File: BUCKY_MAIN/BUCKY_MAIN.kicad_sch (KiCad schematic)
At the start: 23 parts

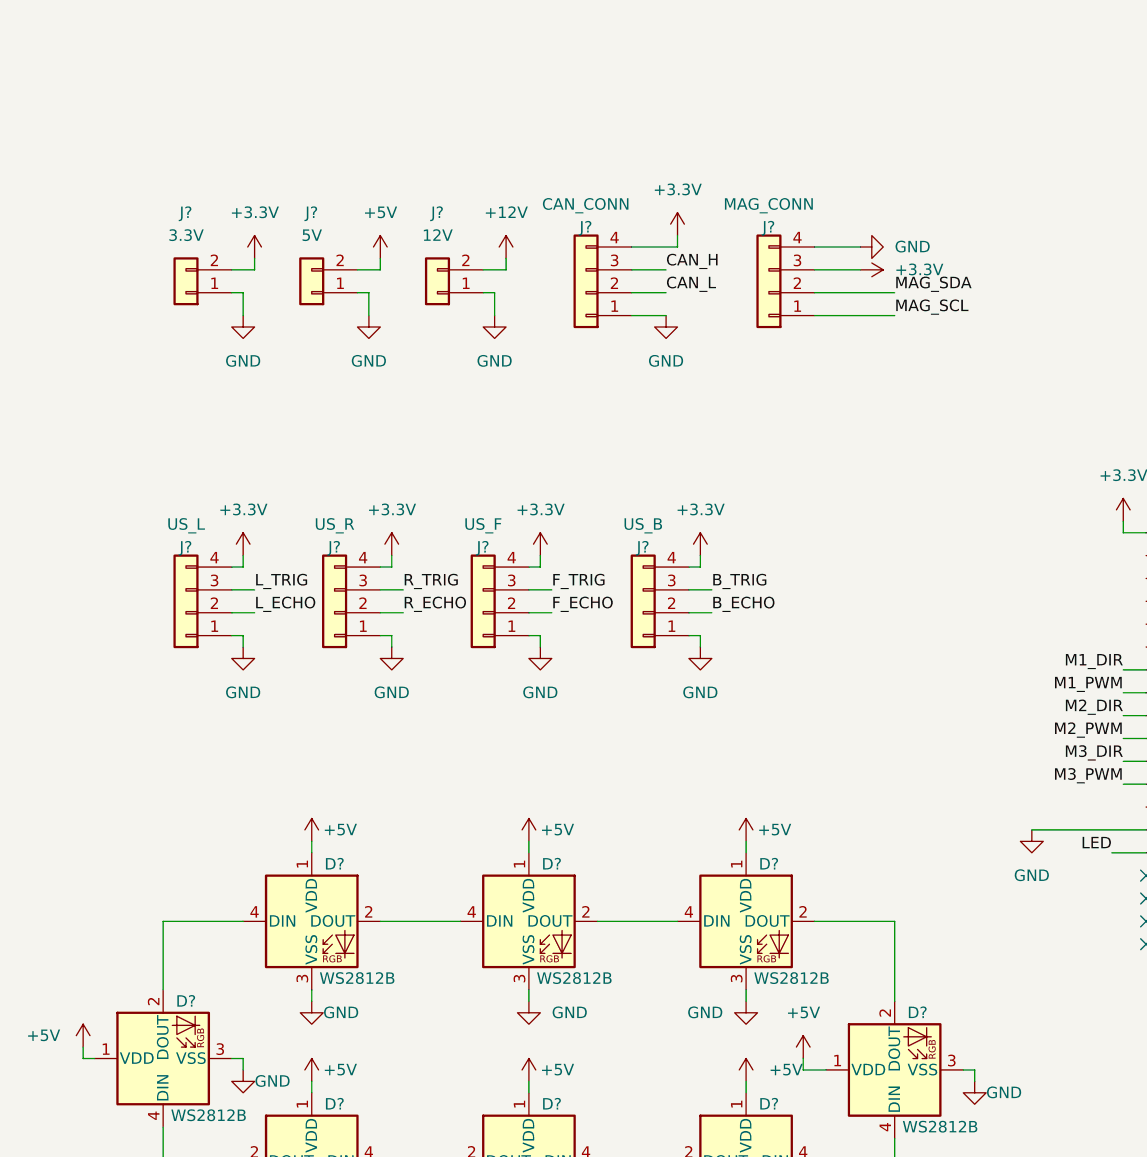
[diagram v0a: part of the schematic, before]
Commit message: Finished Motor Driver Brd
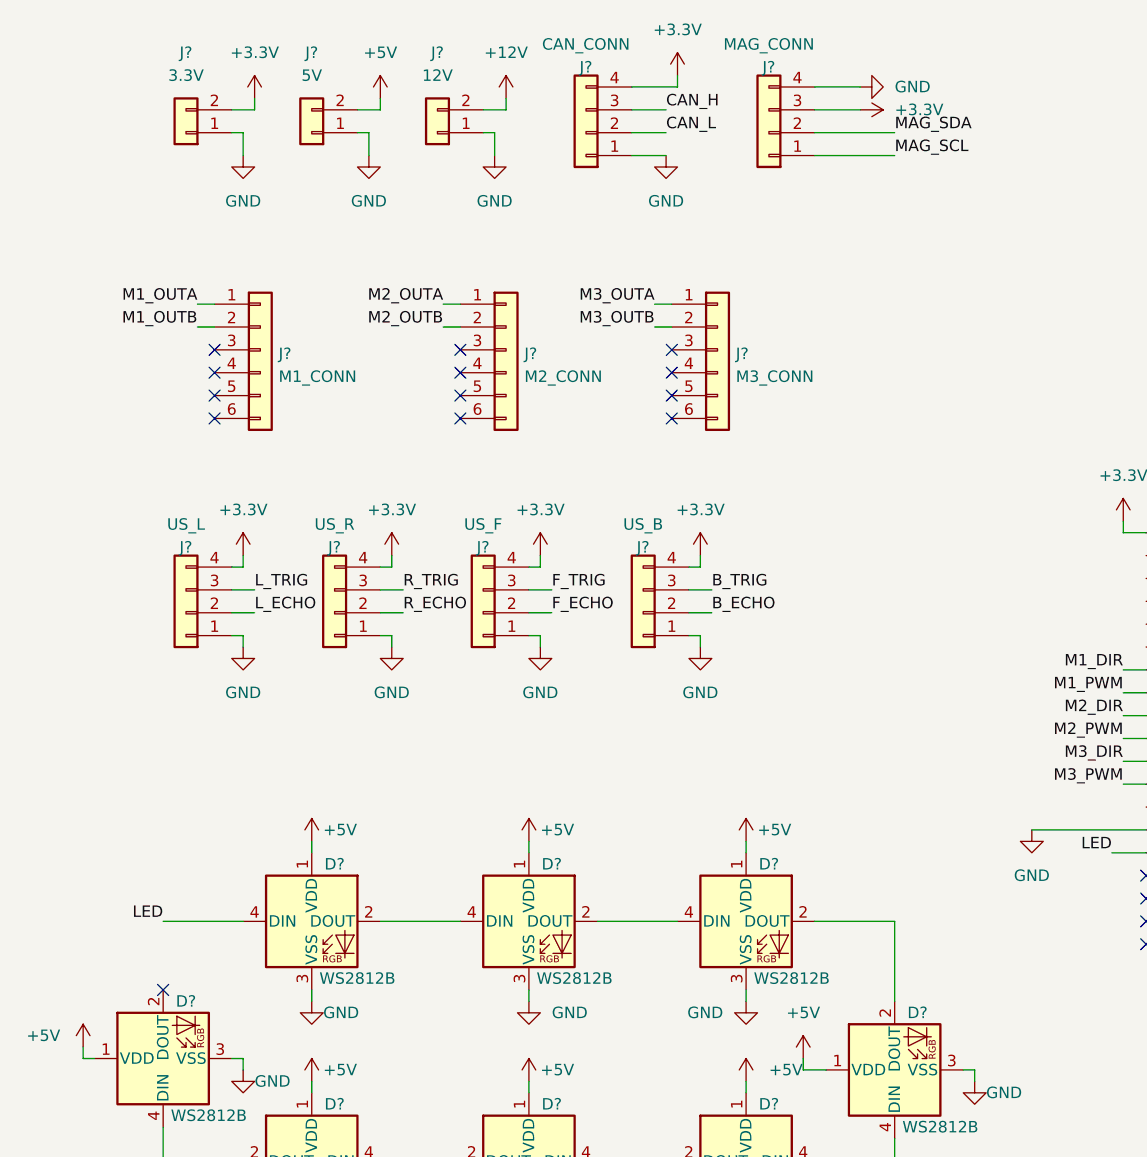
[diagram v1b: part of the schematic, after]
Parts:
- added J?: M3_CONN, symbol Connector_Generic:Conn_01x06
- added J?: M2_CONN, symbol Connector_Generic:Conn_01x06
- added J?: M1_CONN, symbol Connector_Generic:Conn_01x06
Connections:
- net LED: now also D?.4 (DIN)
- net M1_OUTA: now also J?.1 (Pin_1)
- net M1_OUTB: now also J?.2 (Pin_2)
- net M2_OUTA: now also J?.1 (Pin_1)
- net M2_OUTB: now also J?.2 (Pin_2)
- net M3_OUTA: now also J?.1 (Pin_1)
- net M3_OUTB: now also J?.2 (Pin_2)
- net at D?.2 (DOUT): no longer D?.4 (DIN)
- no-connect marks 22 -> 35
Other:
- moved on the sheet: J?

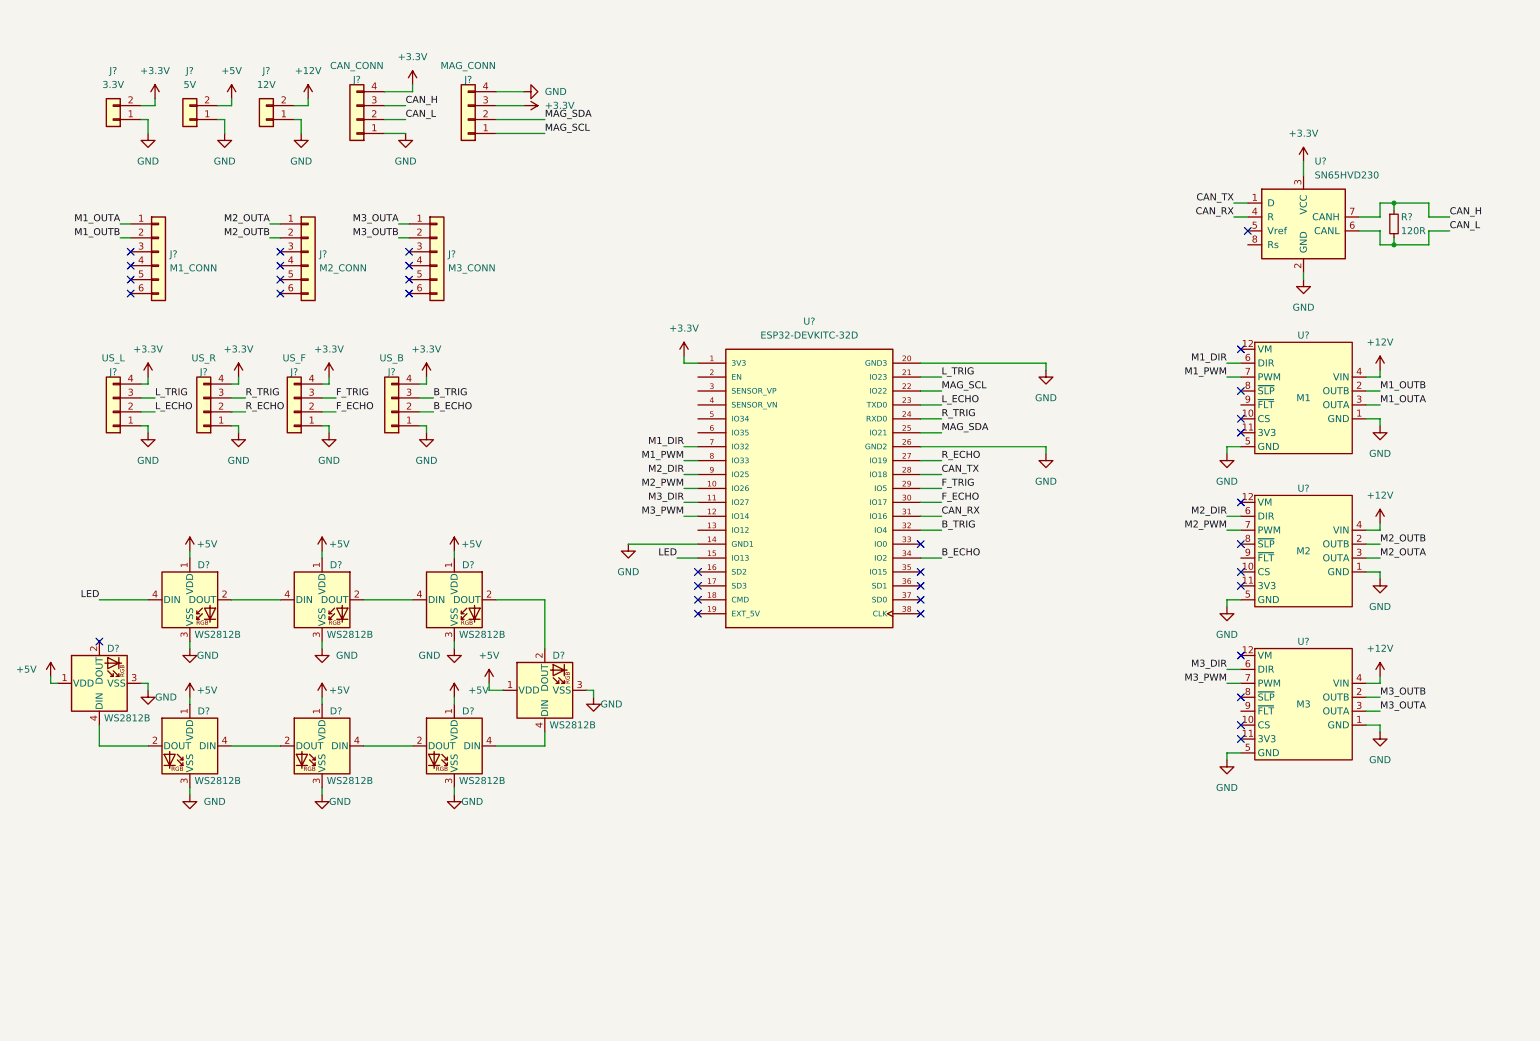
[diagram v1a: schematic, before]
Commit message: Finished up IR sch, Main, Started Power
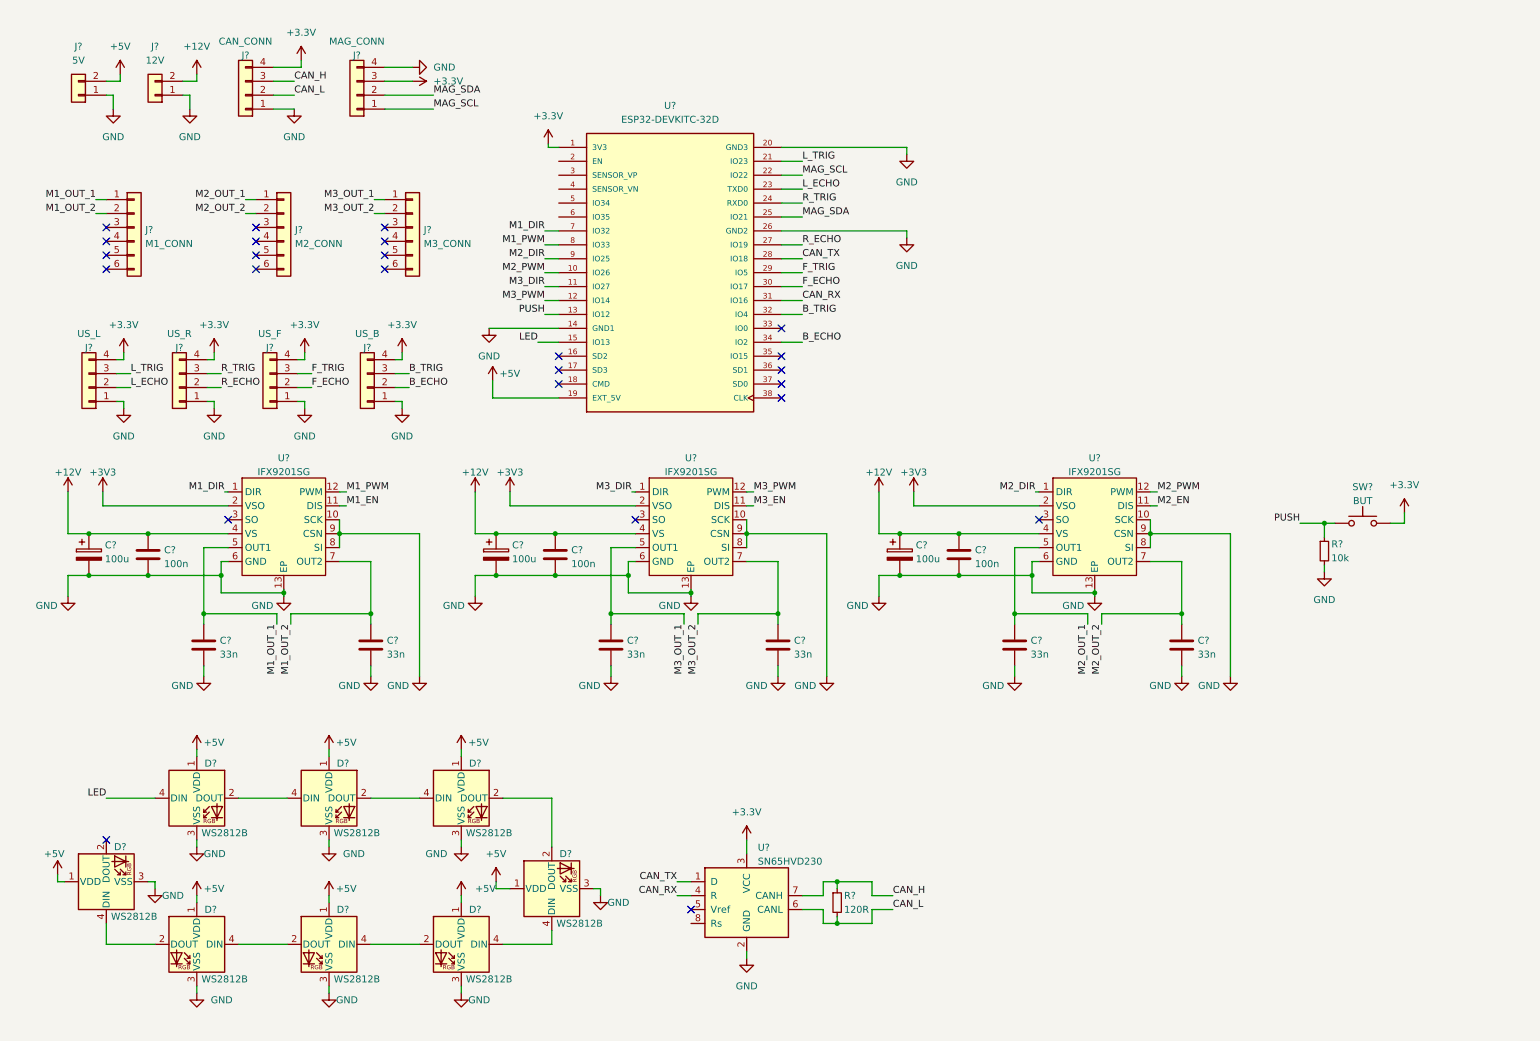
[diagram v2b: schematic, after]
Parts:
- removed J?: 3.3V, symbol Connector_Generic:Conn_01x02
- removed U?: M2, symbol BUCKY_MAIN:G2-24v13
- removed U?: M1, symbol BUCKY_MAIN:G2-24v13
- removed U?: M3, symbol BUCKY_MAIN:G2-24v13
- added C? (x6): 33n, Capacitor_SMD:C_0603_1608Metric_Pad1.08x0.95mm_HandSolder, symbol Device:C
- added C? (x3): 100u, Capacitor_SMD:CP_Elec_6.3x7.7, symbol Device:C_Polarized
- added C? (x3): 100n, Capacitor_SMD:C_0805_2012Metric_Pad1.18x1.45mm_HandSolder, symbol Device:C
- added R?: 10k, symbol Device:R_Small
- added SW?: BUT, symbol Switch:SW_Push
- added U? (x3): IFX9201SG, Package_SO:Infineon_PG-DSO-12-11_ThermalVias, symbol BUCKY_MOTOR_DRIVER:IFX9201SG
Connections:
- net +12V: now also C?.1, C?.1, C?.1, C?.1, C?.1, C?.1, U?.4 (VS), U?.4 (VS), U?.4 (VS)
- net +3.3V: now also SW?.2
- net +5V: now also U?.19 (EXT_5V)
- net GND: now also C?.2, C?.2, C?.2, C?.2, C?.2, C?.2, C?.2, C?.2, C?.2, C?.2, C?.2, C?.2, R?.2, U?.10 (SCK), U?.10 (SCK), U?.10 (SCK), U?.13 (EP), U?.13 (EP), U?.13 (EP), U?.6 (GND), U?.6 (GND), U?.6 (GND), U?.8 (SI), U?.8 (SI), U?.8 (SI), U?.9 (CSN), U?.9 (CSN), U?.9 (CSN)
- net M1_DIR: now also U?.1 (DIR)
- net M1_PWM: now also U?.12 (PWM)
- net M2_DIR: now also U?.1 (DIR)
- net M2_PWM: now also U?.12 (PWM)
- net M3_DIR: now also U?.1 (DIR)
- net M3_PWM: now also U?.12 (PWM)
- net PUSH: now reaches U?.13 (IO12)
- net PUSH: now also R?.1, SW?.1
- net M1_OUTA renamed M1_OUT_1
- net M1_OUT_1: now also C?.1, U?.5 (OUT1)
- net M1_OUTB renamed M1_OUT_2
- net M1_OUT_2: now also C?.1, U?.7 (OUT2)
- net M2_OUTA renamed M2_OUT_1
- net M2_OUT_1: now also C?.1, U?.5 (OUT1)
- net M2_OUTB renamed M2_OUT_2
- net M2_OUT_2: now also C?.1, U?.7 (OUT2)
- net M3_OUTA renamed M3_OUT_1
- net M3_OUT_1: now also C?.1, U?.5 (OUT1)
- net M3_OUTB renamed M3_OUT_2
- net M3_OUT_2: now also C?.1, U?.7 (OUT2)
- new net +3V3: U?.2 (VSO), U?.2 (VSO), U?.2 (VSO)
- new net M1_EN: U?.11 (DIS)
- new net M2_EN: U?.11 (DIS)
- new net M3_EN: U?.11 (DIS)
- no-connect marks 35 -> 25
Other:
- moved on the sheet: D?, J?, R?, U?

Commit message: Started Light PCB
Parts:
- removed J?: CAN_CONN, symbol Connector_Generic:Conn_01x04
- added J?: CAN_CONN, symbol Connector_Generic:Conn_01x06
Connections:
- net +3.3V: now also J?.4 (Pin_4), R?.1, J?.3 (Pin_3); no longer J?.3 (Pin_3), SW?.2
- net +5V: now also J?.1 (Pin_1), J?.2 (Pin_2)
- net CAN_H: now also J?.4 (Pin_4)
- net CAN_L: now also J?.5 (Pin_5)
- net GND: now also J?.1 (Pin_1), SW?.2, J?.6 (Pin_6); no longer J?.4 (Pin_4), R?.2
- net MAG_SCL: now also J?.2 (Pin_2); no longer J?.1 (Pin_1)
- net MAG_SDA: now also J?.3 (Pin_3); no longer J?.2 (Pin_2)
- net PUSH: now also R?.2; no longer R?.1
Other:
- moved on the sheet: J?, R?

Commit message: Started POWER
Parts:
- removed C? (x6): 33n, Capacitor_SMD:C_0603_1608Metric_Pad1.08x0.95mm_HandSolder, symbol Device:C
- removed C? (x3): 100u, Capacitor_SMD:CP_Elec_6.3x7.7, symbol Device:C_Polarized
- removed C? (x3): 100n, Capacitor_SMD:C_0805_2012Metric_Pad1.18x1.45mm_HandSolder, symbol Device:C
- removed U? (x3): IFX9201SG, Package_SO:Infineon_PG-DSO-12-11_ThermalVias, symbol BUCKY_MOTOR_DRIVER:IFX9201SG
- added J?: POWER_CONN, symbol Connector_Generic:Conn_02x04_Top_Bottom
- added J?: OLED_CONN, symbol Connector_Generic:Conn_01x04
- added U? (x3): IFX9201SG_BO, BUCKY_MAIN:IFX9201SG_BO, symbol BUCKY_MAIN:IFX9201SG_BO
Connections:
- net +12V: now also U?.1 (12V), U?.1 (12V), U?.1 (12V), U?.2 (12V), U?.2 (12V), U?.2 (12V)
- net +3.3V: now also J?.4 (Pin_4), U?.8 (3V3), U?.8 (3V3), U?.8 (3V3)
- net GND: now also J?.1 (Pin_1), U?.3 (GND), U?.3 (GND), U?.3 (GND), U?.4 (GND), U?.4 (GND), U?.4 (GND)
- net M1_DIR: now also U?.5 (DIR)
- net M1_OUT_1: now also U?.9 (OUT_A)
- net M1_OUT_2: now also U?.10 (OUT_B)
- net M1_PWM: now also U?.6 (PWM)
- net M2_DIR: now also U?.5 (DIR)
- net M2_OUT_1: now also U?.9 (OUT_A)
- net M2_OUT_2: now also U?.10 (OUT_B)
- net M2_PWM: now also U?.6 (PWM)
- net M3_DIR: now also U?.5 (DIR)
- net M3_OUT_1: now also U?.9 (OUT_A)
- net M3_OUT_2: now also U?.10 (OUT_B)
- net M3_PWM: now also U?.6 (PWM)
- net MAG_SCL renamed SCL
- net SCL: now also J?.2 (Pin_2)
- net MAG_SDA renamed SDA
- net SDA: now also J?.3 (Pin_3)
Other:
- moved on the sheet: R?, SW?

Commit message: Updates to PCB POWER
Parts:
- removed J?: POWER_CONN, symbol Connector_Generic:Conn_02x04_Top_Bottom
- removed J?: 12V, symbol Connector_Generic:Conn_01x02
- removed J?: 5V, symbol Connector_Generic:Conn_01x02
- removed J?: M3_CONN, symbol Connector_Generic:Conn_01x06
- removed J?: M2_CONN, symbol Connector_Generic:Conn_01x06
- removed J?: M1_CONN, symbol Connector_Generic:Conn_01x06
- added J?: M1_CONN, symbol Connector_Generic:Conn_01x06
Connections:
- net +12V: now also J?.3 (Pin_3)
- net +5V: now also J?.2 (Pin_2)
- net GND: now also J?.1 (Pin_1)
- net LED: now also U?.6 (IO35); no longer U?.15 (IO13)
- new net IN: J?.5 (Pin_5)
- new net IS: J?.4 (Pin_4)
- new net ST1: J?.6 (Pin_6)
- no-connect marks 25 -> 17
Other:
- moved on the sheet: J?, R?, SW?

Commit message: POWER Board mag de tyfus krijgen met al die reference designators
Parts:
- removed J?: M1_CONN, symbol Connector_Generic:Conn_01x06
- added J?: PB, symbol Connector_Generic:Conn_01x05
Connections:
- net +12V: now also J?.3 (Pin_3)
- net +5V: now also J?.2 (Pin_2)
- net GND: now also J?.1 (Pin_1)
- net IS: now also U?.35 (IO15), J?.4 (Pin_4)
- net LED: now also U?.13 (IO12); no longer U?.6 (IO35)
- net PUSH: now also U?.6 (IO35); no longer U?.13 (IO12)
- net ST1: now also U?.15 (IO13), J?.5 (Pin_5)
- no-connect marks 17 -> 16
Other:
- moved on the sheet: U?

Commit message: Finished PCBS
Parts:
- J1: renamed from J?; footprint (none) -> BUCKY_MAIN:BUCKY_POWER
- J2, J3, J4, J6, J7: renamed from J?; footprint (none) -> Connector_PinSocket_2.54mm:PinSocket_1x04_P2.54mm_Vertical_SMD_Pin1Left
- J5: renamed from J?; footprint (none) -> Connector_JST:JST_PH_S6B-PH-SM4-TB_1x06-1MP_P2.00mm_Horizontal
- J8: renamed from J?; footprint (none) -> Connector_JST:JST_SH_BM04B-SRSS-TB_1x04-1MP_P1.00mm_Vertical
- R1, R2: renamed from R?; footprint (none) -> Resistor_SMD:R_0805_2012Metric_Pad1.20x1.40mm_HandSolder
- SW1: renamed from SW?; footprint (none) -> BUCKY_MAIN:EVP-BT2J4A000
- gave numbers to parts that had none: 13
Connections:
- net F_ECHO: now also U4.29 (IO5); no longer U4.30 (IO17)
- net F_TRIG: now also U4.30 (IO17); no longer U4.29 (IO5)
- net M1_DIR: now also U4.8 (IO33); no longer U4.7 (IO32)
- net M1_PWM: now also U4.7 (IO32); no longer U4.8 (IO33)
- net M3_DIR: now also U4.12 (IO14); no longer U4.11 (IO27)
- net M3_PWM: now also U4.11 (IO27); no longer U4.12 (IO14)

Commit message: chore: start on schematics
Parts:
- removed D1, D2, D3, D4, D5, D6, D7, D8: WS2812B, LED_SMD:LED_WS2812B_PLCC4_5.0x5.0mm_P3.2mm, symbol LED:WS2812B
- removed J1: PB, BUCKY_MAIN:BUCKY_POWER, symbol Connector_Generic:Conn_01x05
- removed J2: US_L, Connector_PinSocket_2.54mm:PinSocket_1x04_P2.54mm_Vertical_SMD_Pin1Left, symbol Connector_Generic:Conn_01x04
- removed J3: OLED_CONN, Connector_PinSocket_2.54mm:PinSocket_1x04_P2.54mm_Vertical_SMD_Pin1Left, symbol Connector_Generic:Conn_01x04
- removed J4: US_R, Connector_PinSocket_2.54mm:PinSocket_1x04_P2.54mm_Vertical_SMD_Pin1Left, symbol Connector_Generic:Conn_01x04
- removed J5: CAN_CONN, Connector_JST:JST_PH_S6B-PH-SM4-TB_1x06-1MP_P2.00mm_Horizontal, symbol Connector_Generic:Conn_01x06
- removed J6: US_F, Connector_PinSocket_2.54mm:PinSocket_1x04_P2.54mm_Vertical_SMD_Pin1Left, symbol Connector_Generic:Conn_01x04
- removed J7: US_B, Connector_PinSocket_2.54mm:PinSocket_1x04_P2.54mm_Vertical_SMD_Pin1Left, symbol Connector_Generic:Conn_01x04
- removed J8: MAG_CONN, Connector_JST:JST_SH_BM04B-SRSS-TB_1x04-1MP_P1.00mm_Vertical, symbol Connector_Generic:Conn_01x04
- removed R1: 10k, Resistor_SMD:R_0805_2012Metric_Pad1.20x1.40mm_HandSolder, symbol Device:R_Small
- removed R2: 120R, Resistor_SMD:R_0805_2012Metric_Pad1.20x1.40mm_HandSolder, symbol Device:R_Small
- removed SW1: BUT, BUCKY_MAIN:EVP-BT2J4A000, symbol Switch:SW_Push
- removed U4: ESP32-DEVKITC-32D, BUCKY_MAIN:MODULE_ESP32-DEVKITC-32D, symbol ESP32-DEVKITC-32D:ESP32-DEVKITC-32D
- removed U5: SN65HVD230, Package_SO:SOIC-8_3.9x4.9mm_P1.27mm, symbol Interface_CAN_LIN:SN65HVD230
- added D1: D, symbol Device:D
- added J4: Conn_01x10, BUCKY_MAIN:CONN10_S10B-PH_JST, symbol Connector_Generic:Conn_01x10
- added R1, R2: 4700R, Resistor_SMD:R_0402_1005Metric, symbol Device:R
- added R3, R4, R5, R6: 10000R, Resistor_SMD:R_0402_1005Metric, symbol Device:R
- added U4: ~, BUCKY_MAIN:BUCKY_POWER, symbol BUCKY_MAIN:BUCKY_POWER
- added U5, U6, U7, U8: ~, BUCKY_MAIN:BUCKY_TOF, symbol BUCKY_MAIN:BUCKY_TOF
- added U9: PCA9548ADB, DB24, symbol BUCKY_MULTIPLEXER:PCA9548ADB
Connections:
- net +3.3V is gone; now on net +5V: U1.8 (3V3), U2.8 (3V3), U3.8 (3V3)
- net +12V: now also U4.1 (+12V)
- net +5V: now also D1.2 (A), R1.1, R2.1, R3.1, U4.2 (+5V), U5.3 (VCC), U6.3 (VCC), U7.3 (VCC), U8.3 (VCC), U9.24 (VCC)
- net GND: now also J4.10 (Pin_10), R4.1, R5.1, R6.1, U4.3 (-BATT), U4.5 (ST1), U5.4 (GND), U6.4 (GND), U7.4 (GND), U8.4 (GND), U9.12 (GND)
- net M1_DIR: now also U3.5 (DIR), J4.4 (Pin_4); no longer U1.5 (DIR)
- net M1_PWM: now also U3.6 (PWM), J4.3 (Pin_3); no longer U1.6 (PWM)
- net M2_DIR: now also U1.5 (DIR), J4.2 (Pin_2); no longer U2.5 (DIR)
- net M2_PWM: now also U1.6 (PWM), J4.1 (Pin_1); no longer U2.6 (PWM)
- net M3_DIR: now also U2.5 (DIR), J4.6 (Pin_6); no longer U3.5 (DIR)
- net M3_PWM: now also U2.6 (PWM), J4.5 (Pin_5); no longer U3.6 (PWM)
- net SCL: now also J4.8 (Pin_8), R2.2, U9.22 (SCL)
- net SDA: now also J4.7 (Pin_7), R1.2, U9.23 (SDA)
- removed net M1_OUT_1: U1.9 (OUT_A)
- removed net M1_OUT_2: U1.10 (OUT_B)
- removed net M2_OUT_1: U2.9 (OUT_A)
- removed net M2_OUT_2: U2.10 (OUT_B)
- removed net M3_OUT_1: U3.9 (OUT_A)
- removed net M3_OUT_2: U3.10 (OUT_B)
- new net: R4.2, U9.1 (A0)
- new net: D1.1 (K), J4.9 (Pin_9)
- new net: R6.2, U9.21 (A2)
- new net: R3.2, U9.3 (*RESET)
- new net: R5.2, U9.2 (A1)
- new net SCL_0: U5.2 (SCL), U9.5 (SC0)
- new net SCL_1: U6.2 (SCL), U9.7 (SC1)
- new net SCL_2: U7.2 (SCL), U9.9 (SC2)
- new net SCL_3: U8.2 (SCL), U9.11 (SC3)
- new net SDA_0: U5.1 (SDA), U9.4 (SD0)
- new net SDA_1: U6.1 (SDA), U9.6 (SD1)
- new net SDA_2: U7.1 (SDA), U9.8 (SD2)
- new net SDA_3: U8.1 (SDA), U9.10 (SD3)
- no-connect marks 16 -> 12
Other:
- note added: "CONNECTORS (TO BUCKY_PCB/BUCKY_IR)"
- note added: "I2C Multiplexer Creds: Bas de Graaf"
- note added: "MOTOR DRIVERS"
- note added: "POWER CIRCUIT BUCKY_PCB/BUCKY_POWER"
- note added: "TOF SENSORS (DISTANCE)"
- company: PIXELJOCH -> koen1711
